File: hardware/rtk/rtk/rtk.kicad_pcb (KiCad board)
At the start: 2 copper layers, 45 parts, among them J1 USB4105-GF-A, J2 USB4105-GF-A, J3 B2B-PH-SM4-TBLFSN, J5 Conn_Coaxial, J6 MEM2052-00-195-00-A_REVA, J7 Conn_01x04_Pin, U1 BQ24075RGT, U2 TPS63020DSJR, U3 STM32F765VITx, U4 ZED-F9H-01B, U5 ESP32-S3-ZERO, U6 CORE1262-868M, U7 LSM6DSOX

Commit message: Hardware schematic progress: F765 pin assignments, USB HS, TCXO (#182)
- STM32F765VIT pin assignments via CubeMX (rtk-base.ioc updated)
- USB HS hierarchical sheet added (usb2hs.kicad_sch): USB3300 ULPI PHY,
  all 13 ULPI signals wired, reset GPIO, SOF test point
- ASTX-H11-16.000MHZ-T TCXO symbol + footprint added
- USB3300-EZK-TR symbol + footprint added
- USB3300-EZK-TR datasheet added to docs/datasheets/ + catalog updated
- PSU, STM32, ZED-F9P schematic sheets updated
- docs/reference/psu/README.md BQ24075 entry included

Co-Authored-By: Claude Sonnet 4.6 <noreply@anthropic.com>
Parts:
- added C22: 100n, Capacitor_SMD:C_0805_2012Metric_Pad1.18x1.45mm_HandSolder, F.Cu at (106.7, 115.3)
- added C23: 100n, Capacitor_SMD:C_0805_2012Metric_Pad1.18x1.45mm_HandSolder, F.Cu at (106.7, 118.3)
- added C24: 100n, Capacitor_SMD:C_0805_2012Metric_Pad1.18x1.45mm_HandSolder, F.Cu at (106.7, 121.3)
- added C25: 100n, Capacitor_SMD:C_0805_2012Metric_Pad1.18x1.45mm_HandSolder, F.Cu at (106.7, 124.3)
- added C26: 100n, Capacitor_SMD:C_0805_2012Metric_Pad1.18x1.45mm_HandSolder, F.Cu at (130.2, 92.5)
- added J8: Conn_01x01_Pin, Connector_PinHeader_2.54mm:PinHeader_1x01_P2.54mm_Vertical, F.Cu at (154.2, 79.9)
- added J9: Conn_01x08_Pin, Connector_PinHeader_2.54mm:PinHeader_1x08_P2.54mm_Vertical, F.Cu at (155.5, 55.8)
- added U8: USB3300-EZK, Package_DFN_QFN:QFN-32-1EP_5x5mm_P0.5mm_EP3.45x3.45mm, F.Cu at (98.8, 113.6)
- added Y1: ASTX-H11-16.000MHZ-T, ASTX-H11-16.000MHZ-T:XTAL_ASTX-H11-16.000MHZ-T, F.Cu at (130.7, 88.4)
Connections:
- J6 pad P1: unconnected-(J6-DAT2-PadP1) -> SDMMC_D2
- J6 pad P2: unconnected-(J6-CD/DAT3-PadP2) -> SDMMC_D3
- J6 pad P3: unconnected-(J6-CMD-PadP3) -> SDMMC_CMD
- J6 pad P5: unconnected-(J6-CLK-PadP5) -> SDMMC_CK
- J6 pad P7: unconnected-(J6-DAT0-PadP7) -> SDMMC_D0
- J6 pad P8: unconnected-(J6-DAT1-PadP8) -> SDMMC_D1
- J6 pad P9: unconnected-(J6-CD_PIN-PadP9) -> SDMMC_CD
- U3 pad 12: unconnected-(U3-PH0-Pad12) -> RCCCLK
- U3 pad 14: unconnected-(U3-NRST-Pad14) -> NRST
- U3 pad 15: unconnected-(U3-PC0-Pad15) -> HS_ULPI_STP
- U3 pad 16: unconnected-(U3-PC1-Pad16) -> USB3300_RST
- U3 pad 17: unconnected-(U3-PC2-Pad17) -> HS_ULPI_DIR
- U3 pad 18: unconnected-(U3-PC3-Pad18) -> HS_ULPI_NXT
- U3 pad 25: unconnected-(U3-PA3-Pad25) -> HS_ULPI_DO
- U3 pad 28: unconnected-(U3-PA4-Pad28) -> HS_SOF
- U3 pad 29: unconnected-(U3-PA5-Pad29) -> HS_ULPI_CK
- U3 pad 34: unconnected-(U3-PB0-Pad34) -> HS_ULPI_D1
- U3 pad 35: unconnected-(U3-PB1-Pad35) -> HS_ULPI_D2
- U3 pad 37: unconnected-(U3-PE7-Pad37) -> SX1262_UART_RX
- U3 pad 38: unconnected-(U3-PE8-Pad38) -> SX1262_UART_TX
- U3 pad 46: unconnected-(U3-PB10-Pad46) -> HS_ULPI_D3
- U3 pad 47: unconnected-(U3-PB11-Pad47) -> HS_ULPI_D4
- U3 pad 51: unconnected-(U3-PB12-Pad51) -> HS_ULPI_D5
- U3 pad 52: unconnected-(U3-PB13-Pad52) -> HS_ULPI_D6
- U3 pad 53: unconnected-(U3-PB14-Pad53) -> SX1262_SPI2_MISO
- U3 pad 54: unconnected-(U3-PB15-Pad54) -> SX1262_SPI2_MOSI
- U3 pad 55: unconnected-(U3-PD8-Pad55) -> PD8/DEBUG_TX
- U3 pad 56: unconnected-(U3-PD9-Pad56) -> PD9/DEBUG_RX
- U3 pad 58: unconnected-(U3-PD11-Pad58) -> LSM6DSOX_CS
- U3 pad 59: unconnected-(U3-PD12-Pad59) -> I2C4_SCL
- U3 pad 60: unconnected-(U3-PD13-Pad60) -> I2C4_SDA
- U3 pad 61: unconnected-(U3-PD14-Pad61) -> LSM6DSOX_INT1
- U3 pad 62: unconnected-(U3-PD15-Pad62) -> LSM6DSOX_INT2
- U3 pad 65: unconnected-(U3-PC8-Pad65) -> SDMMC_D0
- U3 pad 66: unconnected-(U3-PC9-Pad66) -> SDMMC_D1
- U3 pad 68: unconnected-(U3-PA9-Pad68) -> SX1262_SPI2_SCK
- U3 pad 69: unconnected-(U3-PA10-Pad69) -> SX1262_SPI2_CS
- U3 pad 7: unconnected-(U3-PC13-Pad7) -> SDMMC_CD
- U3 pad 70: unconnected-(U3-PA11-Pad70) -> SX1262_SPI2_RST
- U3 pad 71: unconnected-(U3-PA12-Pad71) -> SX1262_SPI2_BUSY
- U3 pad 72: unconnected-(U3-PA13-Pad72) -> PA13/SWDIO
- U3 pad 76: unconnected-(U3-PA14-Pad76) -> PA14/SWCLK
- U3 pad 78: unconnected-(U3-PC10-Pad78) -> SDMMC_D2
- U3 pad 79: unconnected-(U3-PC11-Pad79) -> SDMMC_D3
- U3 pad 80: unconnected-(U3-PC12-Pad80) -> SDMMC_CK
- U3 pad 83: unconnected-(U3-PD2-Pad83) -> SDMMC_CMD
- U3 pad 89: unconnected-(U3-PB3-Pad89) -> PB3/SWO
- U3 pad 91: unconnected-(U3-PB5-Pad91) -> HS_ULPI_D7
- U3 pad 92: unconnected-(U3-PB6-Pad92) -> SX1262_SPI2_DIO2
- U3 pad 93: unconnected-(U3-PB7-Pad93) -> SX1262_SPI2_DIO1
- U3 pad 94: unconnected-(U3-BOOT0-Pad94) -> BOOT0
- U3 pad 97: unconnected-(U3-PE0-Pad97) -> ESP32_TX
- U3 pad 98: unconnected-(U3-PE1-Pad98) -> ESP32_RX
- U6 pad 10: unconnected-(U6-RESET-Pad10) -> SX1262_SPI2_RST
- U6 pad 11: unconnected-(U6-MISO-Pad11) -> SX1262_SPI2_MISO
- U6 pad 12: unconnected-(U6-MOSI-Pad12) -> SX1262_SPI2_MOSI
- U6 pad 13: unconnected-(U6-CLK-Pad13) -> SX1262_SPI2_SCK
- U6 pad 14: unconnected-(U6-CS-Pad14) -> SX1262_SPI2_CS
- U6 pad 3: unconnected-(U6-RXEN-Pad3) -> SX1262_UART_TX
- U6 pad 4: unconnected-(U6-TXEN-Pad4) -> SX1262_UART_RX
- U6 pad 5: unconnected-(U6-DIO2-Pad5) -> SX1262_SPI2_DIO2
- U6 pad 6: unconnected-(U6-DIO1-Pad6) -> SX1262_SPI2_DIO1
- U6 pad 9: unconnected-(U6-BUSY-Pad9) -> SX1262_SPI2_BUSY
- U7 pad 12: unconnected-(U7-CS-Pad12) -> LSM6DSOX_CS
- U7 pad 13: unconnected-(U7-SCL-Pad13) -> I2C4_SCL
- U7 pad 14: unconnected-(U7-SDA-Pad14) -> I2C4_SDA
- U7 pad 4: unconnected-(U7-INT1-Pad4) -> LSM6DSOX_INT1
- U7 pad 9: unconnected-(U7-INT2-Pad9) -> LSM6DSOX_INT2

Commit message: Schematic progress: all sheets ~90% complete (#182)
- power.kicad_sch: PSU, BQ24075, LiPo connector, USB-C power path
- stm32f765vit.kicad_sch: F765VIT pin assignments, SPI2/I2C4/SDMMC1/UART7/8/USART3
- usb2hs.kicad_sch: USB3300 ULPI, 24MHz TCXO (ASTX-H11-24MHz), USB-C connector, diff pair nets USB_D+/USB_D-
- zed-f9p-05b.kicad_sch: ZED-F9P-05B connections
- rtk-base.ioc: DIO1 corrected to GPIO_Input, LSM6DSOX CS removed (I2C mode, CS tied high in schematic), DIO2 label typo fixed
- rtk.kicad_pcb/pro: project settings updated

Co-Authored-By: Claude Sonnet 4.6 <noreply@anthropic.com>
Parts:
- added C27: 100n, Capacitor_SMD:C_0805_2012Metric_Pad1.18x1.45mm_HandSolder, F.Cu at (128.9, 122.3)
- added C28: 100n, Capacitor_SMD:C_0805_2012Metric_Pad1.18x1.45mm_HandSolder, F.Cu at (128.9, 125.3)
- added C29: 100n, Capacitor_SMD:C_0805_2012Metric_Pad1.18x1.45mm_HandSolder, F.Cu at (128.9, 128.3)
- added C30: 100n, Capacitor_SMD:C_0805_2012Metric_Pad1.18x1.45mm_HandSolder, F.Cu at (128.9, 131.3)
- added L2: 1uH, DFE201610E-1R0M-P2:IND_DFE2016_2X1P6_MUR, F.Cu at (140.8, 122.5)
- added L3: 1uH, DFE201610E-1R0M-P2:IND_DFE2016_2X1P6_MUR, F.Cu at (140.8, 126.0)
- added R10: 10K, Resistor_SMD:R_0805_2012Metric_Pad1.20x1.40mm_HandSolder, F.Cu at (133.7, 125.2)
- added R9: 12k, Resistor_SMD:R_0805_2012Metric_Pad1.20x1.40mm_HandSolder, F.Cu at (133.7, 122.3)
- added Y2: ASTX-H11-24.000MHZ-T, ASTX-H11-16.000MHZ-T:XTAL_ASTX-H11-16.000MHZ-T, F.Cu at (134.2, 129.3)
- moved J7 34.5 mm to (117.5, 126.4)
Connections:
- net I2C_SCK renamed I2C4_SCK
- J1 pad A6: unconnected-(J1-DP1-PadA6) -> USB_D_P
- J1 pad A7: unconnected-(J1-DN1-PadA7) -> USB_D_N
- J1 pad B6: unconnected-(J1-DP2-PadB6) -> USB_D_P
- J1 pad B7: unconnected-(J1-DN2-PadB7) -> USB_D_N
- J7 pad 1: I2C_SDA -> I2C4_SDA
- U3 pad 40: unconnected-(U3-PE10-Pad40) -> F9P_TIMEP
- U3 pad 41: unconnected-(U3-PE11-Pad41) -> F9P_EXTINT
- U3 pad 42: unconnected-(U3-PE12-Pad42) -> F9P_SAFEBOOT_N
- U3 pad 43: unconnected-(U3-PE13-Pad43) -> F9P_RESET_N
- U3 pad 44: unconnected-(U3-PE14-Pad44) -> F9P_D_SEL
- U3 pad 45: unconnected-(U3-PE15-Pad45) -> F9P_TX_READY
- U3 pad 58: LSM6DSOX_CS -> unconnected-(U3-PD11-Pad58)
- U3 pad 95: unconnected-(U3-PB8-Pad95) -> F9P_RX
- U3 pad 96: unconnected-(U3-PB9-Pad96) -> F9P_TX
- U4 pad 33: unconnected-(U4A-VCC-Pad33) -> +3V3
- U4 pad 34: unconnected-(U4A-VCC-Pad34) -> +3V3
- U4 pad 42: unconnected-(U4A-TXD/SPI_MISO-Pad42) -> F9P_RX
- U4 pad 43: unconnected-(U4A-RXD/SPI_MOSI-Pad43) -> F9P_TX
- U4 pad 46: unconnected-(U4A-TX_READY-Pad46) -> F9P_TX_READY
- U4 pad 47: unconnected-(U4A-D_SEL-Pad47) -> F9P_D_SEL
- U4 pad 49: unconnected-(U4A-RESET_N-Pad49) -> F9P_RESET_N
- U4 pad 50: unconnected-(U4A-SAFEBOOT_N-Pad50) -> F9P_SAFEBOOT_N
- U4 pad 51: unconnected-(U4A-EXTINT-Pad51) -> F9P_EXTINT
- U4 pad 7: unconnected-(U4A-VCC_RF-Pad7) -> Net-(U4A-VCC_RF)
- U7 pad 12: LSM6DSOX_CS -> +3V3
- U8 pad 15: unconnected-(U8-VDD1.8-Pad15) -> Net-(C29-Pad1)
- U8 pad 26: unconnected-(U8-VDD1.8-Pad26) -> Net-(C29-Pad1)
- U8 pad 28: unconnected-(U8-XI-Pad28) -> Net-(U8-XI)
- U8 pad 29: unconnected-(U8-VDDA1.8-Pad29) -> Net-(U8-VDDA1.8)
- U8 pad 31: unconnected-(U8-REG_EN-Pad31) -> +3V3
- U8 pad 32: unconnected-(U8-RBIAS-Pad32) -> Net-(U8-RBIAS)
- U8 pad 4: VBUS -> Net-(U8-VBUS)
- U8 pad 7: unconnected-(U8-DP-Pad7) -> USB_D_P
- U8 pad 8: unconnected-(U8-DM-Pad8) -> USB_D_N

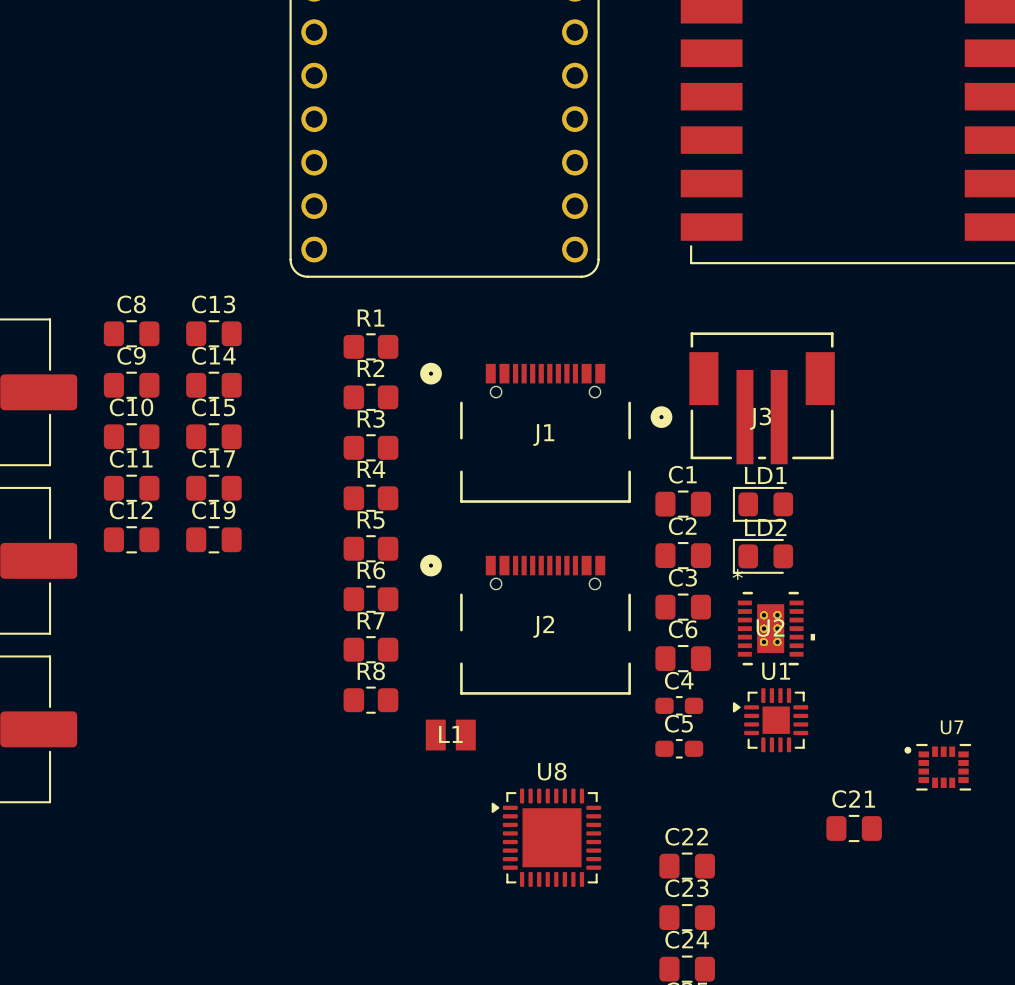
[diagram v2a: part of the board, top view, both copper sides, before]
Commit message: Power sheet review fixes; SLVA553 inrush mitigation added (#182)
- power.kicad_sch: CC1/CC2 5.1k pull-downs on J1+J2, FB divider wiring
  fixed, TPS63020 inrush D1+C_SS per SLVA553, 1M NF bleed resistor
  across C_SS, TS NF 82k5 resistor added, nPGOOD/nCHG net labels added
- stm32f765vit.kicad_sch: nPGOOD→PD10, nCHG→PD11, SYSOFF→PD7 inputs added
- firmware/rtk-base/rtk-base.ioc: PD7/PD10/PD11 assigned
- docs/datasheets/slva553.pdf: TI SLVA553 app note (TPS6302x inrush)

Co-Authored-By: Claude Sonnet 4.6 <noreply@anthropic.com>
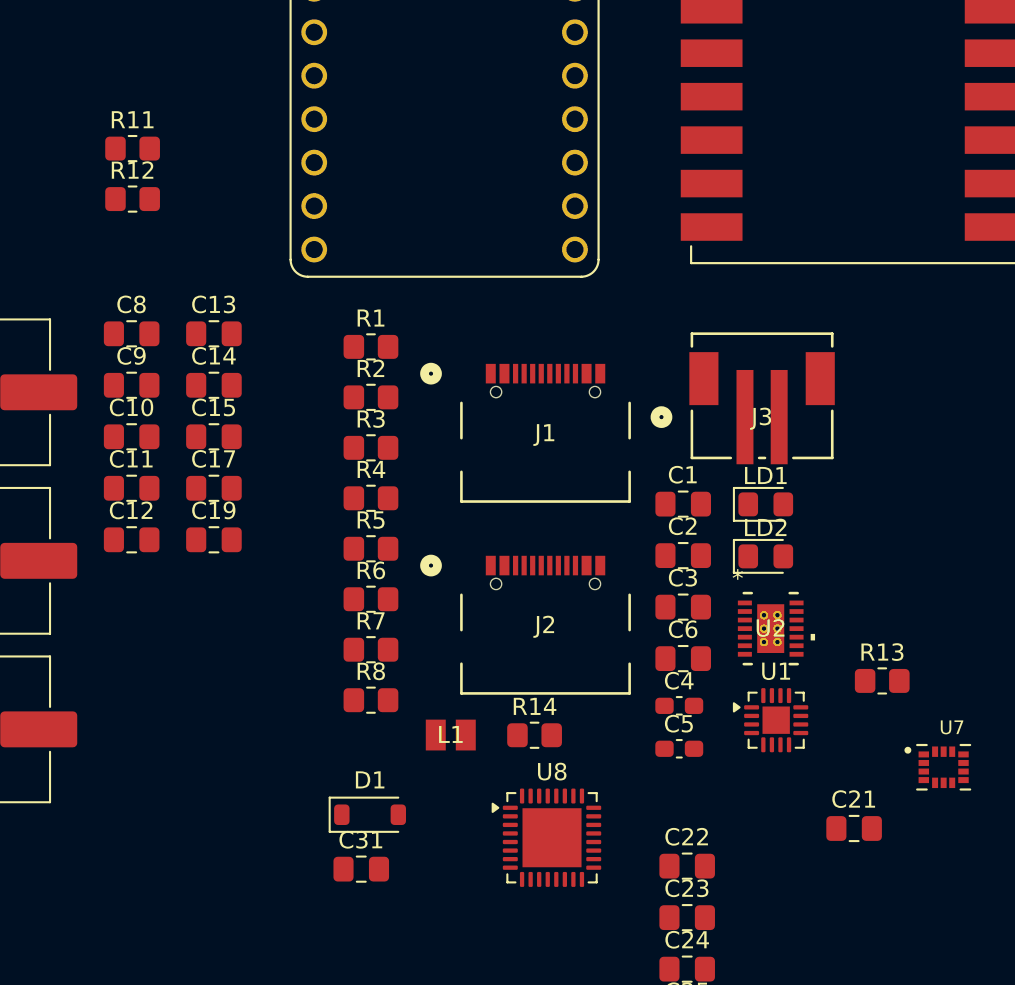
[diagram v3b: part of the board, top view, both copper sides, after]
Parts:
- added C31: 10n, Capacitor_SMD:C_0805_2012Metric_Pad1.18x1.45mm_HandSolder, F.Cu at (87.6, 115.5)
- added D1: 1N4148W, Diode_SMD:D_SOD-123, F.Cu at (88.1, 112.3)
- added R11: 5k1, Resistor_SMD:R_0805_2012Metric_Pad1.20x1.40mm_HandSolder, F.Cu at (74.3, 73.4)
- added R12: 5k1, Resistor_SMD:R_0805_2012Metric_Pad1.20x1.40mm_HandSolder, F.Cu at (74.3, 76.3)
- added R13: NF or 82k5, Resistor_SMD:R_0805_2012Metric_Pad1.20x1.40mm_HandSolder, F.Cu at (118.1, 104.5)
- added R14: NF or 1M, Resistor_SMD:R_0805_2012Metric_Pad1.20x1.40mm_HandSolder, F.Cu at (97.8, 107.7)
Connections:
- J1 pad A5: unconnected-(J1-CC1-PadA5) -> Net-(J1-CC1)
- J1 pad B5: unconnected-(J1-CC2-PadB5) -> Net-(J1-CC2)
- R7 pad 1: +3V3 -> Net-(D1-K)
- R7 pad 2: Net-(U2-FB) -> +3V3
- R8 pad 2: +3V3 -> Net-(D1-K)
- U1 pad 1: unconnected-(U1-TS-Pad1) -> Net-(U1-TS)
- U2 pad 3: Net-(U2-FB) -> Net-(D1-K)
- U3 pad 32: unconnected-(U3-PC4-Pad32) -> F9P_ANT_DETECT
- U3 pad 33: unconnected-(U3-PC5-Pad33) -> F9P_ANT_OFF
- U3 pad 36: unconnected-(U3-PB2-Pad36) -> F9P_ANT_SHORT
- U3 pad 57: unconnected-(U3-PD10-Pad57) -> nPGOOD
- U3 pad 58: unconnected-(U3-PD11-Pad58) -> nCHG
- U3 pad 88: unconnected-(U3-PD7-Pad88) -> SYSOFF
- U4 pad 19: unconnected-(U4A-GEOFENCE_STAT-Pad19) -> F9P_GEOFENCE_STAT
- U4 pad 20: unconnected-(U4A-RTK_STAT-Pad20) -> F9P_RTK_STAT
- U4 pad 4: unconnected-(U4A-ANT_DETECT-Pad4) -> F9P_ANT_DETECT
- U4 pad 5: unconnected-(U4A-ANT_OFF-Pad5) -> F9P_ANT_OFF
- U4 pad 6: unconnected-(U4A-ANT_SHORT_N-Pad6) -> F9P_ANT_SHORT

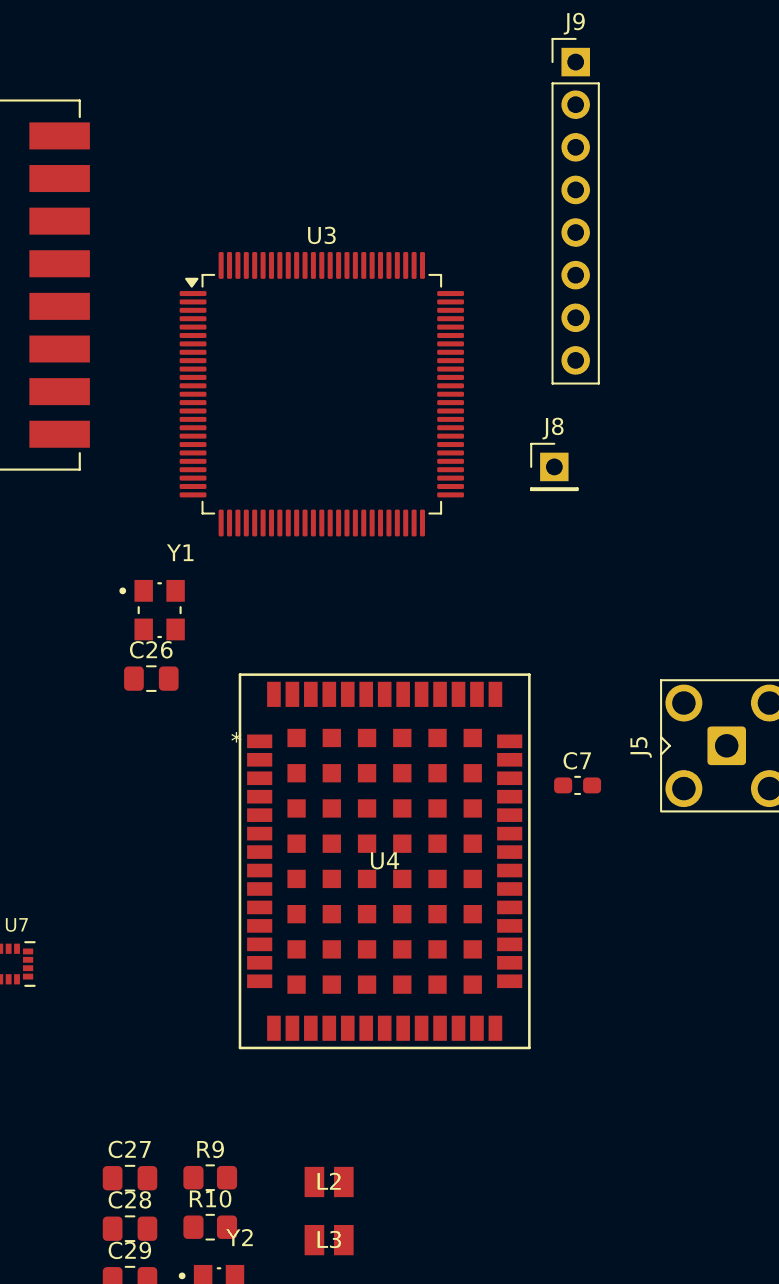
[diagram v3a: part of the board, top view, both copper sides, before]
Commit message: STM32F765VIT sheet review fixes (#182)
- VBAT tied to +3V3 (not raw LiPo)
- CORE1262 RXEN/TXEN reassigned to PC6/PC7 GPIO outputs (init low)
- I2C4 external 4k7 pull-ups added on SCL/SDA
- BOOT0 pull-down + test point added
- LSM6DSOX CS tied to +3V3, SDO/SA0 tied to GND (addr 0x6A)
- ESP32-S3-ZERO: 5V NC, powered via 3V3 rail; GP1-GP5 wired to PE2-PE6
- nPGOOD/nCHG/SYSOFF added to STM32 sheet
- MMC5603NJ sub-board connector added (I2C4, 2x GPIO, 3V3, GND)
- rtk-base.ioc: PC6/PC7 RXEN/TXEN, PE2-PE6 spare, PD7/PD10/PD11

Co-Authored-By: Claude Sonnet 4.6 <noreply@anthropic.com>
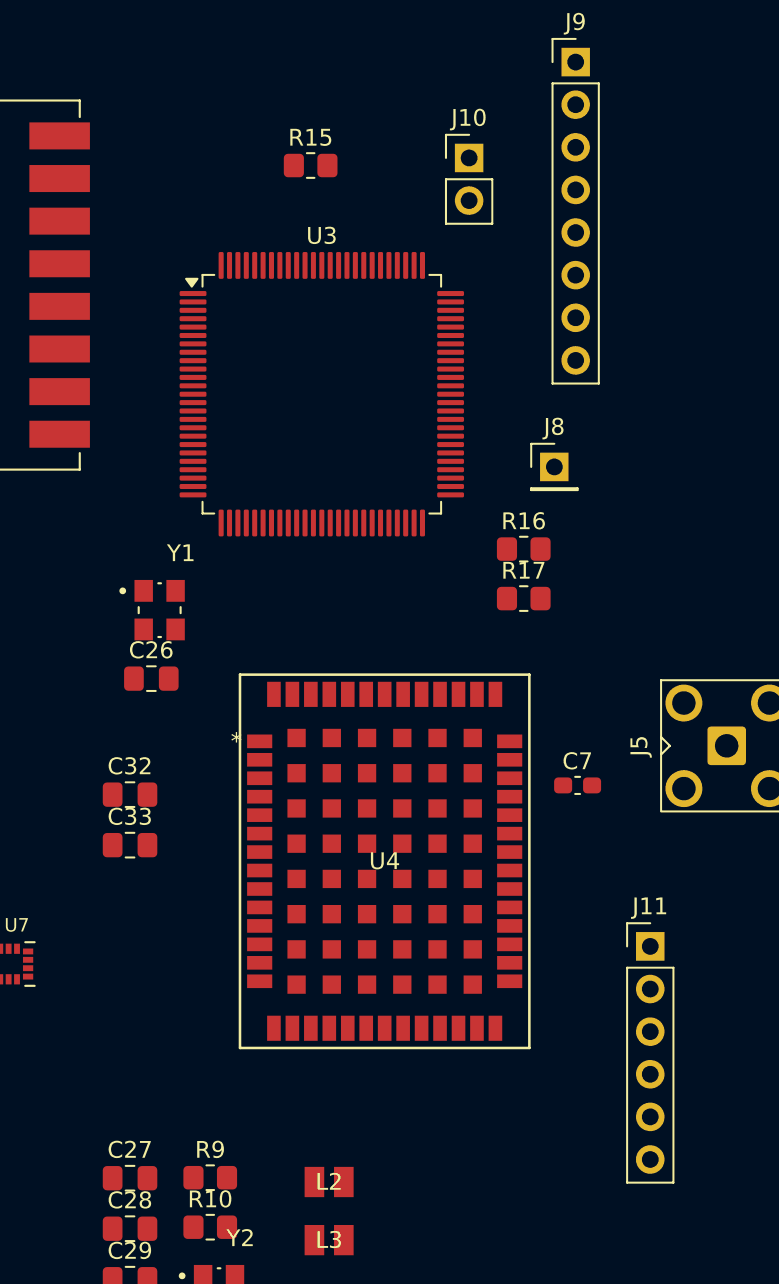
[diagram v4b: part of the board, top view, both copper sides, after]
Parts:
- added C32: 1u, Capacitor_SMD:C_0805_2012Metric_Pad1.18x1.45mm_HandSolder, F.Cu at (128.9, 99.4)
- added C33: 1u, Capacitor_SMD:C_0805_2012Metric_Pad1.18x1.45mm_HandSolder, F.Cu at (128.9, 102.4)
- added J10: Conn_01x02_Pin, Connector_PinHeader_2.54mm:PinHeader_1x02_P2.54mm_Vertical, F.Cu at (149.1, 61.5)
- added J11: Conn_01x06_Pin, Connector_PinHeader_2.54mm:PinHeader_1x06_P2.54mm_Vertical, F.Cu at (159.9, 108.5)
- added R15: 1k, Resistor_SMD:R_0805_2012Metric_Pad1.20x1.40mm_HandSolder, F.Cu at (139.7, 61.9)
- added R16: 4k7, Resistor_SMD:R_0805_2012Metric_Pad1.20x1.40mm_HandSolder, F.Cu at (152.4, 84.8)
- added R17: 4k7, Resistor_SMD:R_0805_2012Metric_Pad1.20x1.40mm_HandSolder, F.Cu at (152.4, 87.7)
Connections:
- C8 pad 1: VBAT -> +3V3
- J3 pad 1: VBAT -> /Power/VBAT
- U3 pad 1: unconnected-(U3-PE2-Pad1) -> ESP32_GP1
- U3 pad 2: unconnected-(U3-PE3-Pad2) -> ESP32_GP2
- U3 pad 3: unconnected-(U3-PE4-Pad3) -> ESP32_GP3
- U3 pad 37: SX1262_UART_RX -> MAGNETO_SPARE1
- U3 pad 38: SX1262_UART_TX -> MAGNETO_SPARE2
- U3 pad 4: unconnected-(U3-PE5-Pad4) -> ESP32_GP4
- U3 pad 48: unconnected-(U3-VCAP_1-Pad48) -> Net-(U3-VCAP_1)
- U3 pad 5: unconnected-(U3-PE6-Pad5) -> ESP32_GP5
- U3 pad 6: VBAT -> +3V3
- U3 pad 63: unconnected-(U3-PC6-Pad63) -> SX1262_RXEN
- U3 pad 64: unconnected-(U3-PC7-Pad64) -> SX1262_TXEN
- U3 pad 73: unconnected-(U3-VCAP_2-Pad73) -> Net-(U3-VCAP_2)
- U5 pad 1: unconnected-(U5-GP1-Pad1) -> ESP32_GP1
- U5 pad 2: unconnected-(U5-GP2-Pad2) -> ESP32_GP2
- U5 pad 3: unconnected-(U5-GP3-Pad3) -> ESP32_GP3
- U5 pad 4: unconnected-(U5-GP4-Pad4) -> ESP32_GP4
- U5 pad 5: unconnected-(U5-GP5-Pad5) -> ESP32_GP5
- U6 pad 3: SX1262_UART_TX -> SX1262_RXEN
- U6 pad 4: SX1262_UART_RX -> SX1262_TXEN
- U7 pad 1: unconnected-(U7-SDO/SA0-Pad1) -> GND
